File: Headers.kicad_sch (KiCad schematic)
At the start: 10 parts, among them J1 PPTC082LFBN-RC, J13 Conn_01x20

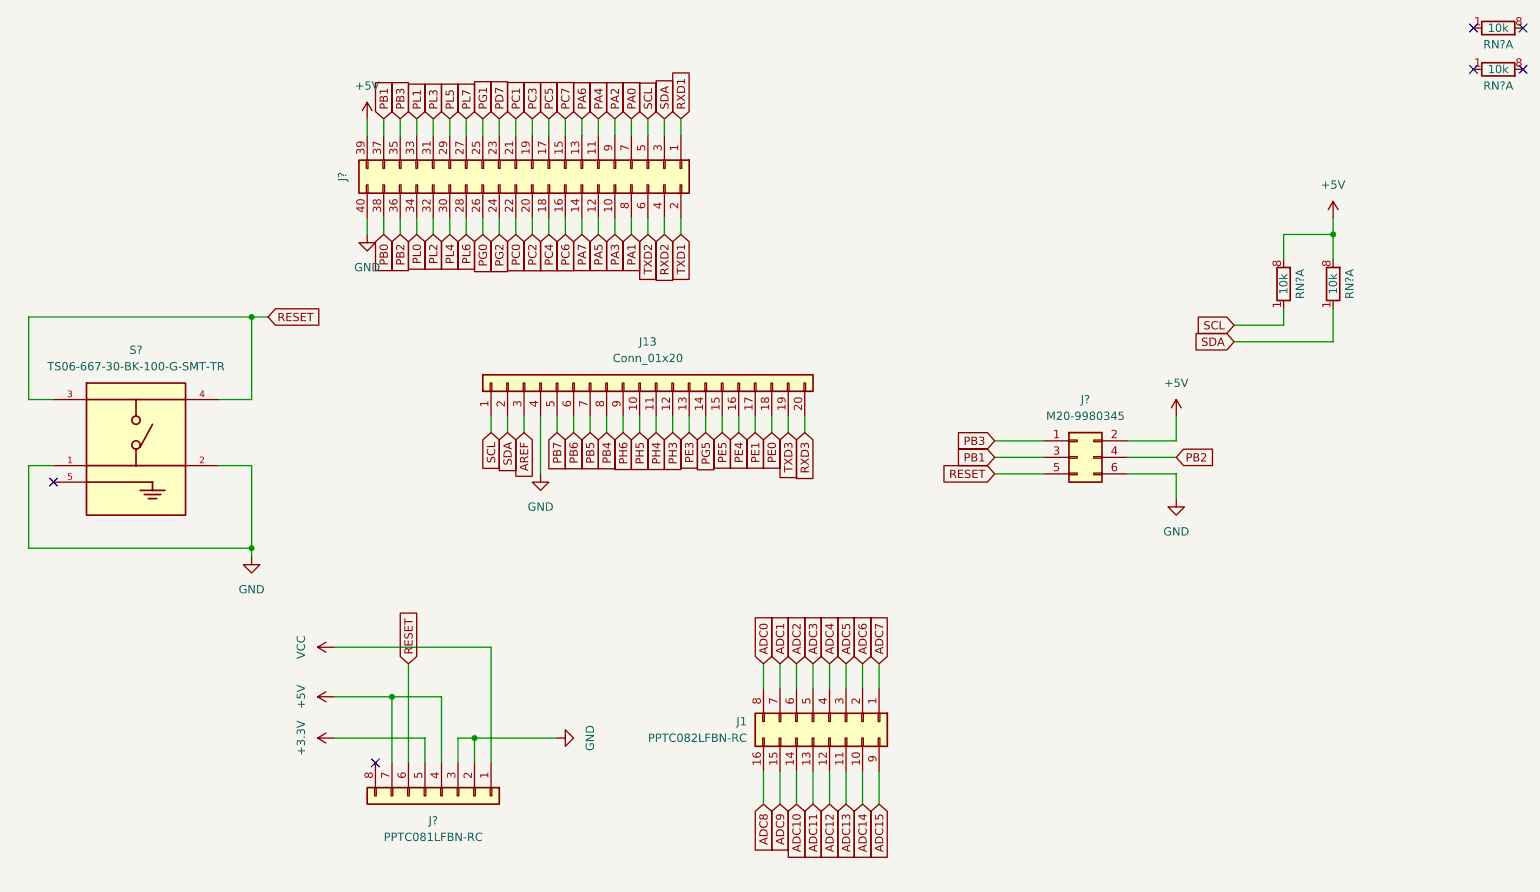
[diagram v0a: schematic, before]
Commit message: WIP, replace bottom headers
replaced the two bottom headers with one big 2x16 header.
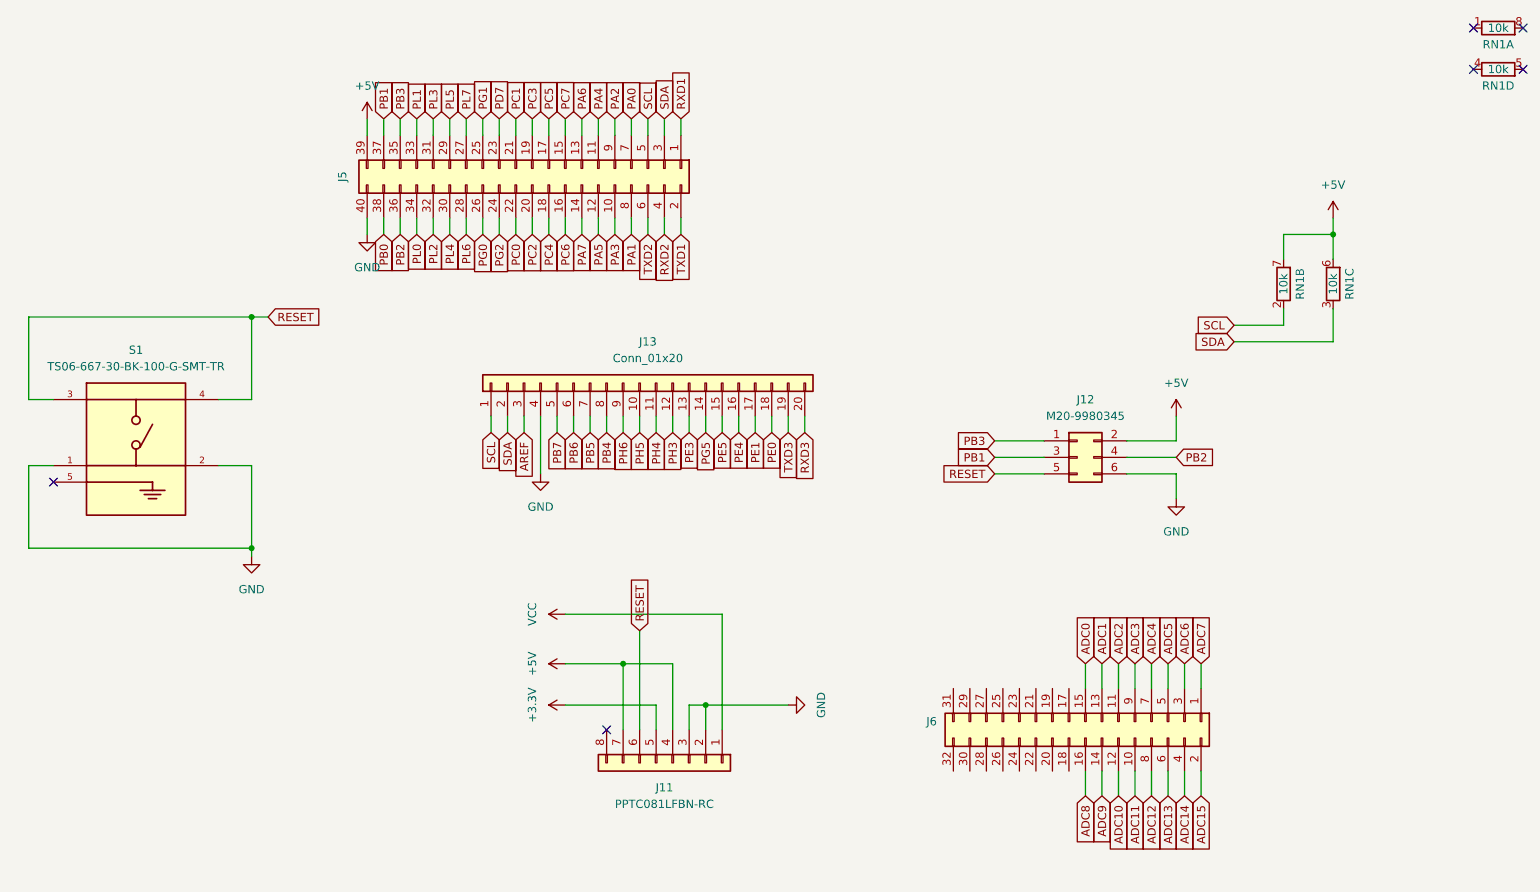
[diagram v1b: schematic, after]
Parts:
- removed J1: PPTC082LFBN-RC, Connector_PinSocket_2.54mm:PinSocket_2x08_P2.54mm_Vertical, symbol Connector_Generic:Conn_02x08_Top_Bottom
- added J6: Conn_02x16_Top_Bottom, Connector_PinSocket_2.54mm:PinSocket_2x16_P2.54mm_Vertical, symbol Connector_Generic:Conn_02x16_Odd_Even
- gave numbers to parts that had none: 5
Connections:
- net +5V: now also RN1.6 (R3.2), RN1.7 (R2.2); no longer RN1.8 (R1.2), RN1.8 (R1.2)
- net ADC0: now also J6.15 (Pin_15)
- net ADC1: now also J6.13 (Pin_13)
- net ADC10: now also J6.12 (Pin_12)
- net ADC11: now also J6.10 (Pin_10)
- net ADC12: now also J6.8 (Pin_8)
- net ADC13: now also J6.6 (Pin_6)
- net ADC14: now also J6.4 (Pin_4)
- net ADC15: now also J6.2 (Pin_2)
- net ADC2: now also J6.11 (Pin_11)
- net ADC3: now also J6.9 (Pin_9)
- net ADC4: now also J6.7 (Pin_7)
- net ADC5: now also J6.5 (Pin_5)
- net ADC6: now also J6.3 (Pin_3)
- net ADC7: now also J6.1 (Pin_1)
- net ADC8: now also J6.16 (Pin_16)
- net ADC9: now also J6.14 (Pin_14)
- net SCL: now also RN1.2 (R2.1); no longer RN1.1 (R1.1)
- net SDA: now also RN1.3 (R3.1); no longer RN1.1 (R1.1)
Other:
- moved on the sheet: J11

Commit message: Continued work
almost complete
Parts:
- removed J11: PPTC081LFBN-RC, Connector_PinSocket_2.54mm:PinSocket_1x08_P2.54mm_Vertical, symbol Connector_Generic:Conn_01x08
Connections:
- net +3.3V: now also J6.25 (Pin_25), J6.26 (Pin_26)
- net +5V: now also J6.27 (Pin_27), J6.28 (Pin_28), J6.29 (Pin_29), J6.30 (Pin_30), J6.31 (Pin_31)
- net GND: now also J6.19 (Pin_19), J6.20 (Pin_20), J6.21 (Pin_21), J6.22 (Pin_22), J6.23 (Pin_23), J6.24 (Pin_24)
- net RESET: now also J6.32 (Pin_32)
- net VCC: now also J6.17 (Pin_17), J6.18 (Pin_18)
- no-connect marks 6 -> 5
